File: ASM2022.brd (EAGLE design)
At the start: 28.3 x 26.5 mm, 43 parts, among them J1 SM02B-SRSS-TB(LF)(SN), J2 47346-0001, J3 EVP-ANDA1A, J4 EVP-ANDA1A, J5 EVP-ANDA1A, J6 DF12-32-DP, J7 EVP-ANDA1A, Q1 DMP2035U, SW1 PCM12SMTR, U1 XC6210B33, U2 MCP73831, U3 UG-9664HDDAG01, U4 FAN5340, U5 ATSAMD21G18A, Y1 32.7680

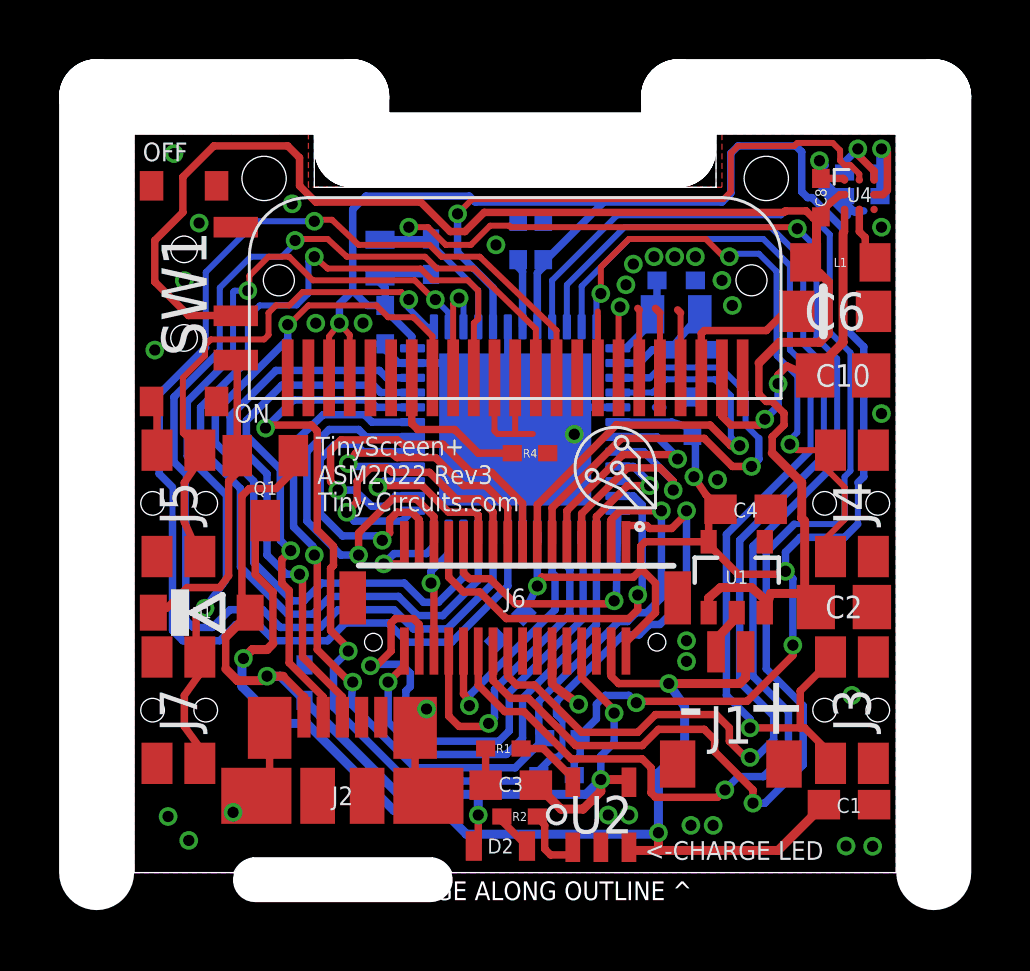
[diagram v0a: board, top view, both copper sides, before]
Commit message: Update to Rev 4 PCB
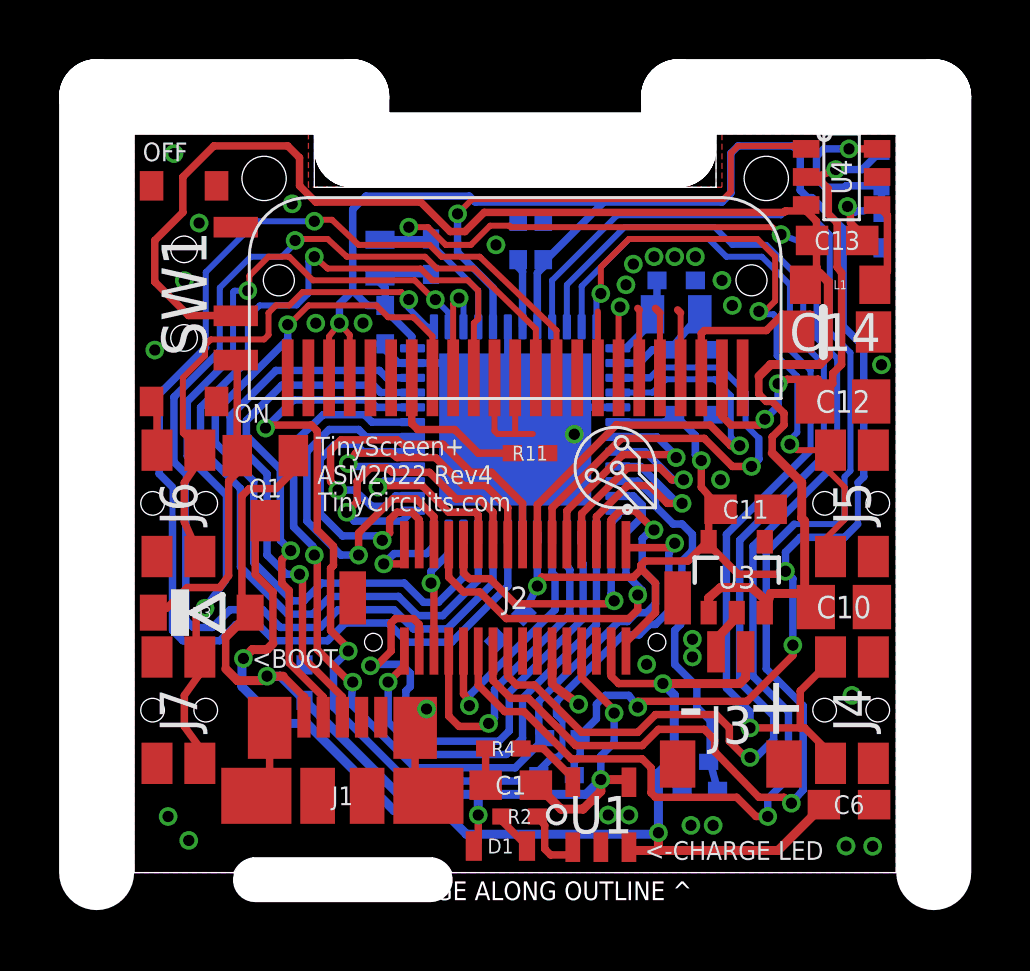
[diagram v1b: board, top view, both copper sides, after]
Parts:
- added R10: 1.00M, tinycircuits:0402
- added R11: 1.2M, tinycircuits:0402
- C1: value 4.7uF -> 10uF
- C11, C13: value .1uF -> 10uF; device tinycircuits:C0402 -> tinycircuits:C0603
- C12: value .1uF -> 10uF; device tinycircuits:C0402 -> tinycircuits:C0805
- C14: value .1uF -> 4.7uF; device tinycircuits:C0402 -> tinycircuits:1206_CAP_TANT
- C2: value 10uF -> 22pF; device tinycircuits:C0805 -> tinycircuits:C0402
- C3: value 10uF -> 22pF; device tinycircuits:C0603 -> tinycircuits:C0402
- C4: value 10uF -> .1uF; device tinycircuits:C0603 -> tinycircuits:C0402
- C5, C7: value 22pF -> .1uF
- C6: device tinycircuits:1206_CAP_TANT -> tinycircuits:C0603
- C8: value 4.7uF -> .1uF
- D1: value MBR120 -> AMBER; device tinycircuits:SOD-123FL -> tinycircuits:LNJ_LED
- D2: value AMBER -> CD0603; device tinycircuits:LNJ_LED -> tinycircuits:0603
- D3: value CD0603 -> MBR120; device tinycircuits:0603 -> tinycircuits:SOD-123FL
- J1: value SM02B-SRSS-TB(LF)(SN) -> 47346-0001; device tinycircuits:JST_SH_2X1 -> tinycircuits:MICRO_USB
- J2: value 47346-0001 -> DF12-32-DP; device tinycircuits:MICRO_USB -> tinycircuits:DF12-32-DP
- J3: value EVP-ANDA1A -> SM02B-SRSS; device tinycircuits:PTS840GKP -> tinycircuits:JST_SH_2X1
- J4, J5, J7: value EVP-ANDA1A -> PTS840GKP
- J6: value DF12-32-DP -> PTS840GKP; device tinycircuits:DF12-32-DP -> tinycircuits:PTS840GKP
- R1: value 5K -> 10K
- R3: value 100k -> 10K
- R4: value 1.2M -> 5K
- R5: value 115k -> 100k
- R6: value 4.7k -> 10K
- R7, R9: value 10K -> 1.00M
- R8: value 10K -> 16K
- U1: value XC6210B33 -> MCP73831; device tinycircuits:SOT-25 -> tinycircuits:SOT-23
- U2: value MCP73831 -> ATSAMD21G18A; device tinycircuits:SOT-23 -> tinycircuits:QFN48
- U3: value UG-9664HDDAG01 -> XC6210B33; device tinycircuits:OLED_DISPLAY -> tinycircuits:SOT-25
- U4: value FAN5340 -> AP3036B; device tinycircuits:WLCSP8_1_57X1_57 -> tinycircuits:SOT-23-6
- U5: value ATSAMD21G18A -> UG-9664HDDAG01; device tinycircuits:QFN48 -> tinycircuits:OLED_DISPLAY
- moved R5 25.6 mm to (12.9, 11.4), turned to 270 degrees
- moved R7 23.3 mm to (32.4, 28.9), turned to 90 degrees
- moved J5 22.8 mm to (31.4, 17.5), turned to 90 degrees
- moved D2 20.3 mm to (15.4, 25.8), flipped to the bottom
- moved R8 20.3 mm to (32.4, 26.8), turned to 90 degrees
- moved R9 19.2 mm to (25.9, 8.75), turned to 0 degrees
- moved C6 16.7 mm to (31.3, 7.30)
- moved C3 15.9 mm to (25.9, 22.7), flipped to the bottom
- moved C8 15.4 mm to (15.6, 23.6), flipped to the bottom, turned to 270 degrees
- moved C14 15.2 mm to (30.8, 23.3), flipped to the top, turned to 0 degrees
- moved R6 14.7 mm to (17.1, 25.9), turned to 270 degrees
- moved C12 13.6 mm to (31.1, 20.9), flipped to the top, turned to 0 degrees
- moved D3 13.4 mm to (9.39, 13.8), flipped to the top, turned to 0 degrees
- moved J1 13.4 mm to (14.2, 7.60), turned to 90 degrees
- moved U2 13.4 mm to (20.0, 20.0), flipped to the bottom
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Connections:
- removed net AD4/SDA: J6.3, R8.1, U5.31
- removed net AD5/SCL: J6.1, R7.1, U5.32
- removed net N$13: R5.1, U4.A3
- removed net N$9: L1.2, U4.C2
- new net N$4: L1.2, U4.4
- new net SCL: J2.1, R1.1, U2.32
- new net SDA: J2.3, R3.1, U2.31
- net +12V: now also C12.1, R7.2, U4.2, U5.22; no longer C10.1, U3.22, U4.C1
- net +3V3: now also J2.6; no longer J6.6
- net +5V: now also C1.1, D3.A, J1.1, J2.8, R5.2, U1.4; no longer C3.1, D2.A, J2.1, J6.8, R3.2, U2.4
- net AD0: now also J2.11, U2.3; no longer J6.11, U5.3
- net AD1: now also J2.9, U2.7; no longer J6.9, U5.7
- net AD2: now also J2.7, U2.8; no longer J6.7, U5.8
- net AD3: now also J2.5, U2.9; no longer J6.5, U5.9
- net AD4: now also R10.2, R9.1, U2.10; no longer U5.10
- net AD5: now also J4.1, J4.2, U2.47; no longer J3.1, J3.2, U5.47
- net AREF: now also J2.13, U2.4; no longer J6.13, U5.4
- net ATN/IO38: now also U2.22, U5.8; no longer U3.8, U5.22
- net DBG_RXD: now also U2.38; no longer U5.38
- net DBG_TXD: now also J6.1, J6.2, U2.37; no longer J5.1, J5.2, U5.37
- net GND: now also J1.5, J1.P1, J1.P2, J1.P3, J1.P4, J1.P5, J1.P6, J2.12, J2.14, J3.1, J6.3, J6.4, R10.1, R11.1, R4.2, R5.1, R8.1, U2.18, U2.35, U2.42, U2.5, U2.EXP, U4.5, U5.11, U5.12, U5.16, U5.17, U5.19, U5.2, U5.20, U5.6; no longer J1.1, J2.5, J2.P1, J2.P2, J2.P3, J2.P4, J2.P5, J2.P6, J3.3, J3.4, J6.12, J6.14, R1.2, R3.1, R4.1, R6.1, U2.2, U3.11, U3.12, U3.16, U3.17, U3.18, U3.19, U3.20, U3.5, U3.6, U4.A1, U4.C3, U5.35, U5.42, U5.EXP
- net IO0: now also J2.24, U2.16; no longer J6.24, U5.16
- net IO1: now also J2.26, U2.15; no longer J6.26, U5.15
- net IO2: now also J2.28, U2.23; no longer J6.28, U5.23
- net IO3: now also J2.30, U2.14; no longer J6.30, U5.14
- net IO4: now also J2.32, U2.13; no longer J6.32, U5.13
- net IO5: now also J2.31, U2.24; no longer J6.31, U5.24
- net IO6: now also J2.29, U2.29; no longer J6.29, U5.29
- net IO7: now also J2.27, U2.30; no longer J6.27, U5.30
- net IO8: now also J2.25, U2.11; no longer J6.25, U5.11
- net IO9: now also J2.23, U2.12; no longer J6.23, U5.12
- net MISO: now also J2.17, U2.28; no longer J6.17, U5.28
- net MISO_ALT: now also U2.21, U5.10; no longer U3.10, U5.21
- net MOSI: now also J2.19, U2.25; no longer J6.19, U5.25
- net MOSI_ALT: now also U2.19, U5.14; no longer U3.14, U5.19
- net N$1: now also C2.1, U2.1; no longer C5.1, U5.1
- net N$11: now also R11.2, U5.7; no longer R4.2, U3.7
- net N$12: now also C14.1, U5.21; no longer C6.1, U3.21
- net N$15: now also U5.15; no longer U3.15
- net N$2: now also D3.C; no longer D1.C
- net N$3: now also C3.1, U2.2; no longer C7.1, U5.2
- net N$5: now also D1.C; no longer D2.C
- net N$6: now also R4.1, U1.5; no longer R1.1, U2.5
- net N$7: now also U1.1; no longer U2.1
- net N$8: now also U2.43; no longer U5.43
- net RESET: now also D2.A, J2.22, R6.1, U2.40; no longer D3.A, J6.22, R9.1, U5.40
- net RSV2: now also J2.16; no longer J6.16
- net RX_LED/IO25/AIN11: now also J5.1, J5.2, U2.48; no longer J4.1, J4.2, U5.48
- net SCK: now also J2.15, U2.26; no longer J6.15, U5.26
- net SCK_ALT: now also U2.20, U5.13; no longer U3.13, U5.20
- net SS: now also J2.21, U2.27; no longer J6.21, U5.27
- net SWCLK: now also J2.20, U2.45; no longer J6.20, U5.45
- net SWDIO: now also J2.18, U2.46; no longer J6.18, U5.46
- net TX_LED/IO26: now also U2.39, U5.9; no longer U3.9, U5.39
- net USB_HOST_EN/IO27: now also U2.41, U4.1; no longer U4.A2, U5.41
- net USB_N: now also J1.2, U2.33; no longer J2.2, U5.33
- net USB_P: now also J1.3, U2.34; no longer J2.3, U5.34
- net VBATT: now also C6.1, J2.4, J3.2, R9.2, U1.3; no longer C1.1, J1.2, J6.4, U2.3
- net VCC: now also C5.1, C7.1, C8.1, D2.C, J2.2, R1.2, R3.2, R6.2, U2.17, U2.36, U2.44, U2.6, U3.5, U5.3, U5.4; no longer C12.1, C13.1, C14.1, D3.C, J6.2, R7.2, R8.2, R9.2, U1.5, U3.3, U3.4, U5.17, U5.36, U5.44, U5.6
- net VCC_IN: now also C10.1, C13.1, U3.1, U3.3, U4.3; no longer C2.1, C8.1, U1.1, U1.3, U4.B1
- net VIN: now also J2.10; no longer J6.10
- net V_FB: now also R7.1, R8.2, U4.6; no longer R5.2, R6.2, U4.B3
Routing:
- net AD5/SCL: track 40.3 -> 0.00 mm, vias 3 -> 0
- net SCL: track 0.00 -> 37.9 mm, vias 0 -> 3
- net AD4/SDA: track 35.0 -> 0.00 mm, vias 3 -> 0
- net SDA: track 0.00 -> 34.4 mm, vias 0 -> 3
- net AD4: track 0.00 -> 13.0 mm
- net +12V: track 13.0 -> 18.1 mm, vias 2 -> 3
- net GND: track 53.2 -> 48.4 mm, vias 35 -> 34
- net N$4: track 0.00 -> 3.02 mm
- net USB_HOST_EN/IO27: track 20.5 -> 17.9 mm
- net AD3: track 4.59 -> 7.23 mm
- net V_FB: track 3.66 -> 6.15 mm
- net N$13: track 2.26 -> 0.00 mm, vias 1 -> 0
- net N$9: track 2.03 -> 0.00 mm
- net RESET: track 54.4 -> 55.7 mm
- net RX_LED/IO25/AIN11: track 21.0 -> 21.9 mm
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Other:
- board text added: "4"
- board text added: "<BOOT"
- board text added: "ASM2022 Rev4"
- board text added: "TinyCircuits.com"
- board text removed: "3"
- board text removed: "ASM2022 Rev3"
- board text removed: "Tiny-Circuits.com"
